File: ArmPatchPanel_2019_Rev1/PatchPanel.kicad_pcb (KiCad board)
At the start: 2 copper layers, 61 x 100.1 mm, 5 parts

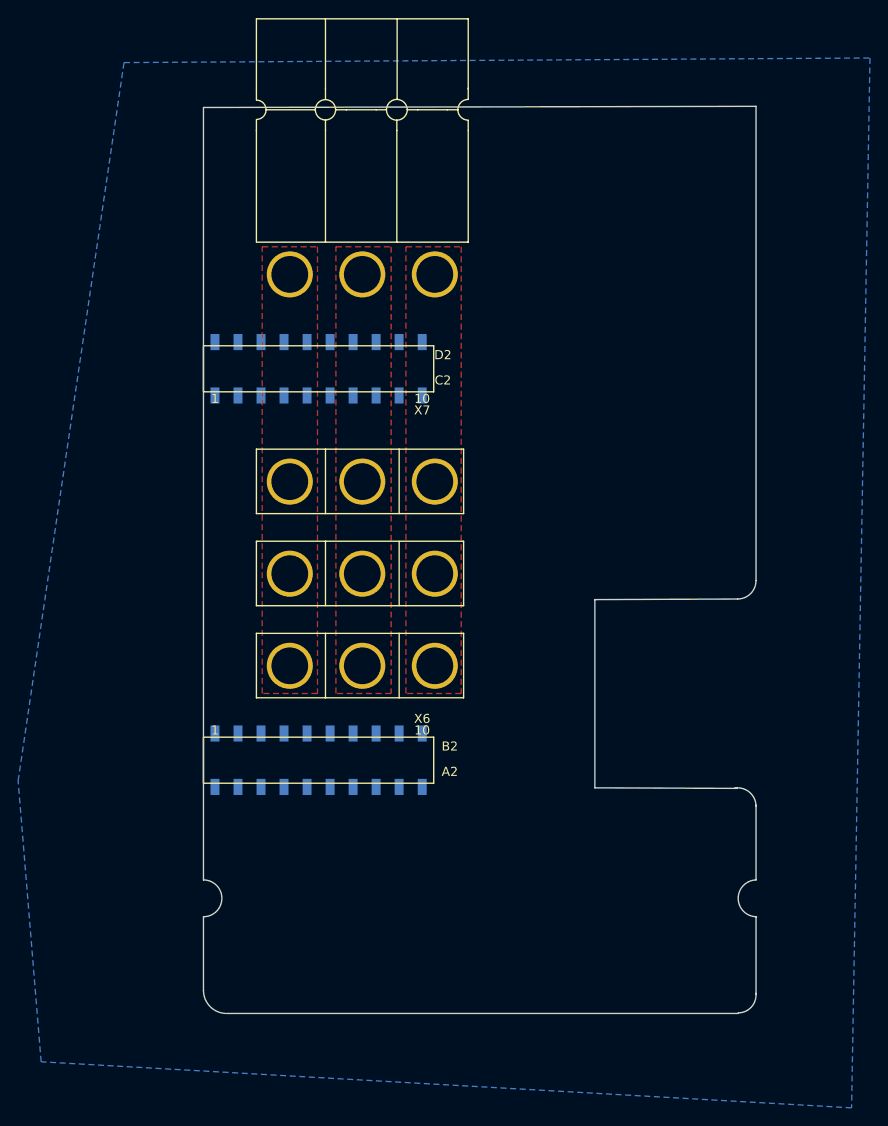
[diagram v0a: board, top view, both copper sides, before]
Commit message: added another molex2 on patch panel
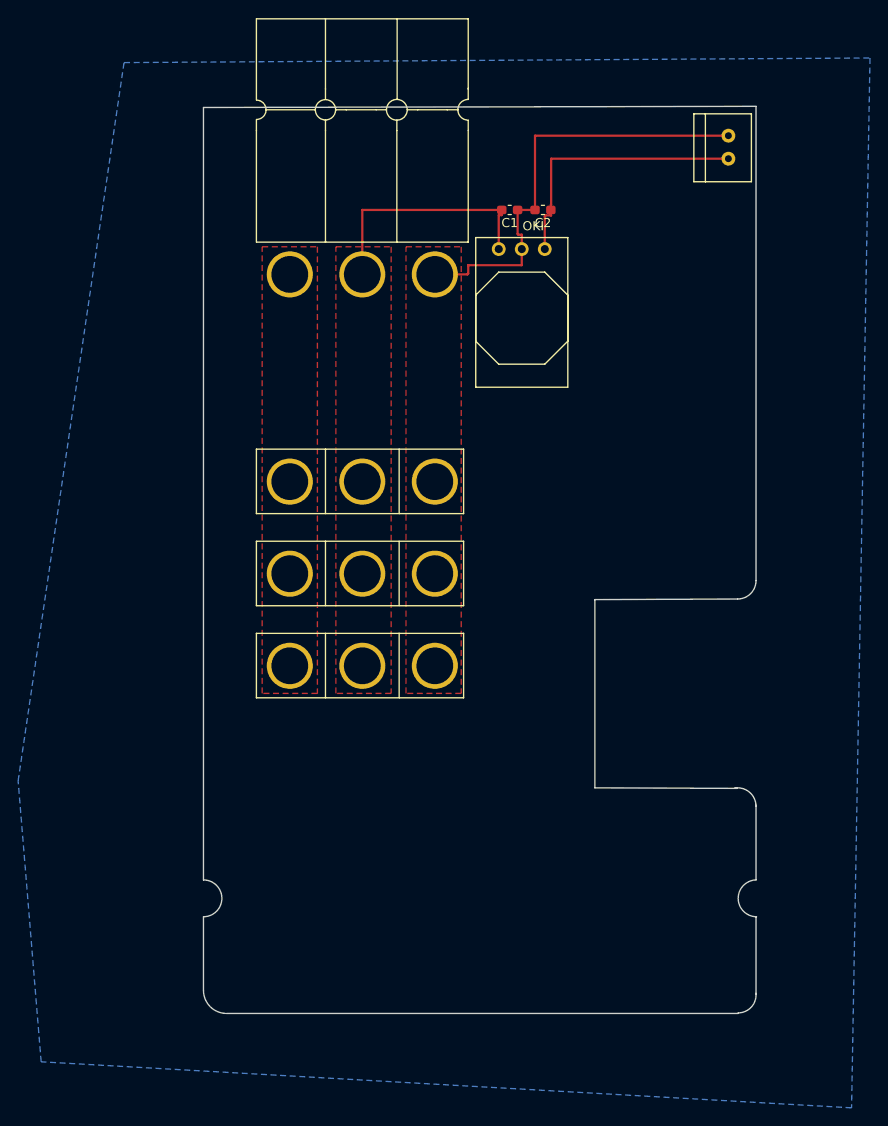
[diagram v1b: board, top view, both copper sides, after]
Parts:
- removed REF**: TM4C129E_Launchpad_X7, MRDT_Shields:TM4C129E_Launchpad_X7_Bottom_SMD
- added C1: 10uF, Capacitor_SMD:C_0603_1608Metric_Pad1.05x0.95mm_HandSolder, F.Cu at (146.2, 25.9)
- added C2: 10uF, Capacitor_SMD:C_0603_1608Metric_Pad1.05x0.95mm_HandSolder, F.Cu at (149.8, 25.9)
- added Conn5: Molex_SL_02, MRDT_Connectors:MOLEX_SL_02_Vertical, F.Cu at (170.3, 19.0)
- added U1: OKI, MRDT_Devices:OKI_Horizontal, F.Cu at (142.4, 29.0)
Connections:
- net Net-(Conn1-Pad1) renamed /GND
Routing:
- net /GND: track 0.00 -> 48.5 mm
- net /+5V: track 0.00 -> 30.2 mm
- net Net-(C1-Pad2): track 0.00 -> 27.1 mm
